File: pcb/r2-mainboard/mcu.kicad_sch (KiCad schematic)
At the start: 28 parts, among them J20 SWD+JTAG (DNP), Q9 AO3400A, SW20 EVQPUC02K, SW21 SW, SW22 SW, U20 STM32G0B1RCT6, Y20 32.768kHz

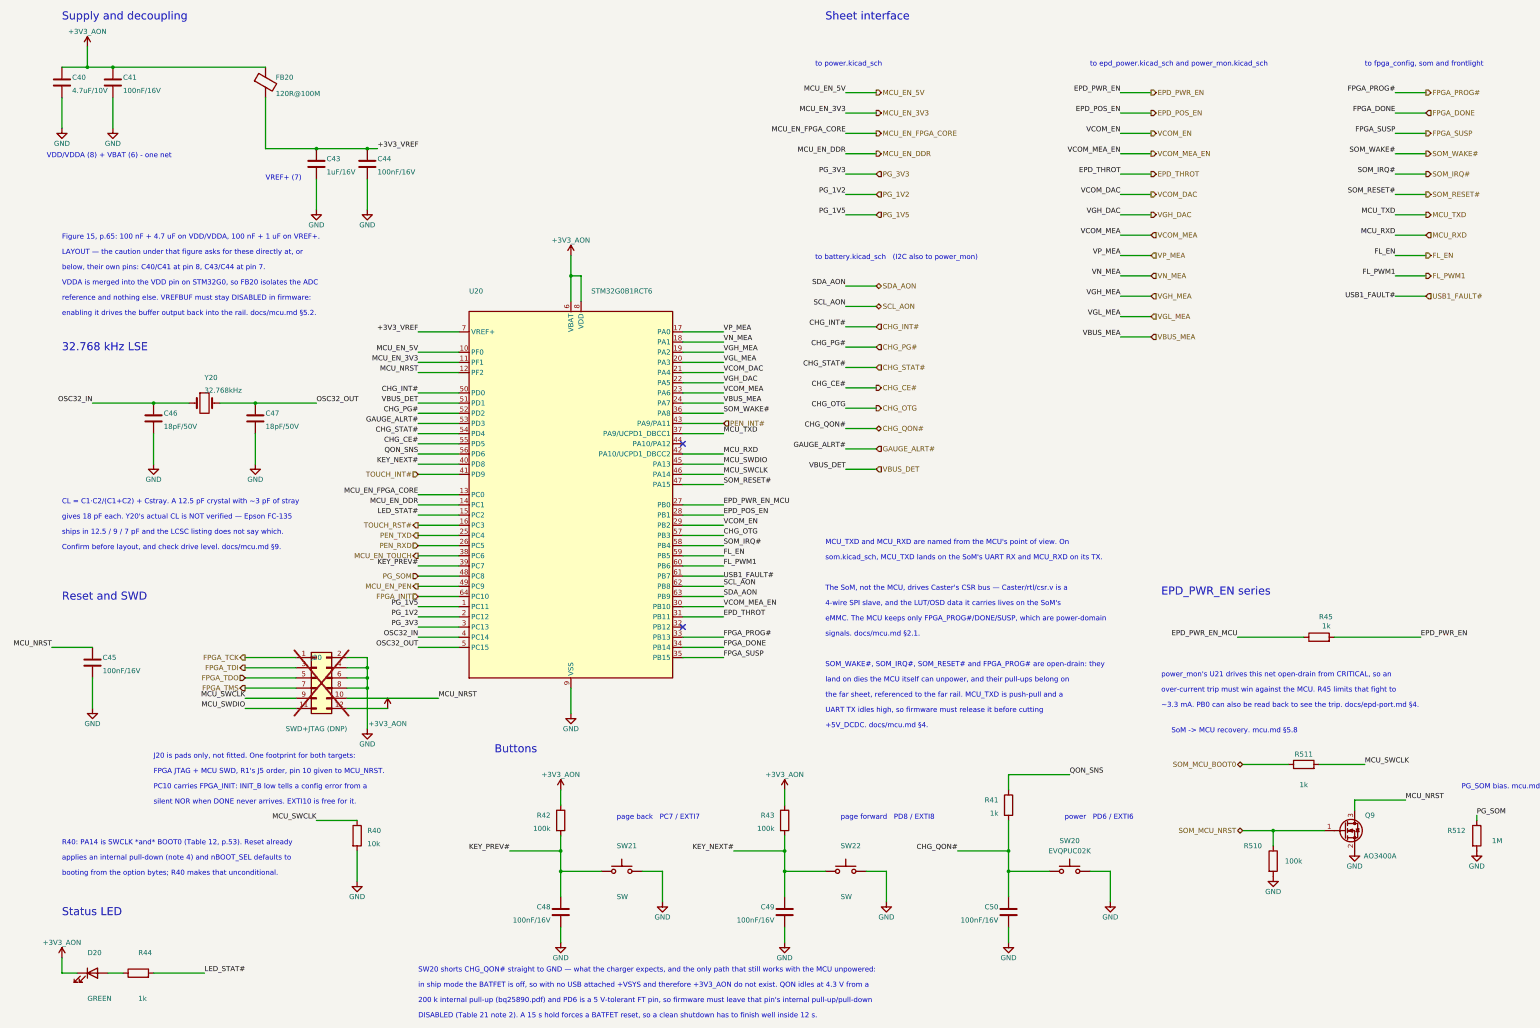
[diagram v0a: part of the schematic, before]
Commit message: R2: renumber every sheet to the page-based designator scheme
The owner's scheme is classifier + sheet page + two-digit part from 00. Four
sheets already used it; this converts the remaining nine, so all thirteen now
agree: pages 2-9 take three digits, pages 10-14 four. 292 of 333 designators
changed. A part shared by several sheets takes its lowest page, so the FPGA is
U700 (pages 7-9) and the two SoM connectors are J501/J502 (pages 5-6).

The whole risk here is silently rewiring the board, so the netlist was diffed
rather than eyeballed:

  nets 519 -> 519, total pin connections 1563 -> 1563
  named nets present in both whose pin multiset changed: 0
  ERC unchanged at 14 errors / 20 warnings
  check_ucf.py: 99 balls matched, 0 failures

That last one matters most: it resolves the gateware's 113 UCF constraints to
board nets *by ball name*, so it is the sharpest detector of the corruption
this change could cause.

Two earlier attempts did cause exactly that. A bare quoted-string substitution
also rewrites FPGA ball names (C1, D2, N11, T1) and BTH-060 pin names (A1-D60),
which are spelled exactly like designators; one run left ERC identical while 40
nets came back with a different pin multiset. The tool now substitutes only at
the two positions that store an instance's designator, and excludes every pin
name everywhere else. docs/layout.md 9.5 records the hazard and how to prove a
renumber was clean.

Only the three scripts that read the design are updated. The gen_*/patch_*/
port_r1.py scripts keep the old names deliberately: each wrote a sheet once and
has not been re-runnable since it was hand-edited in Eeschema, so they are a
historical record -- and port_r1.py's dict keys are R1 designators that were
never renumbered at all.

Co-Authored-By: Claude Opus 5 <noreply@anthropic.com>
Claude-Session: https://claude.ai/code/session_01MHTAe6ZnhogTEgtyPcLhwG
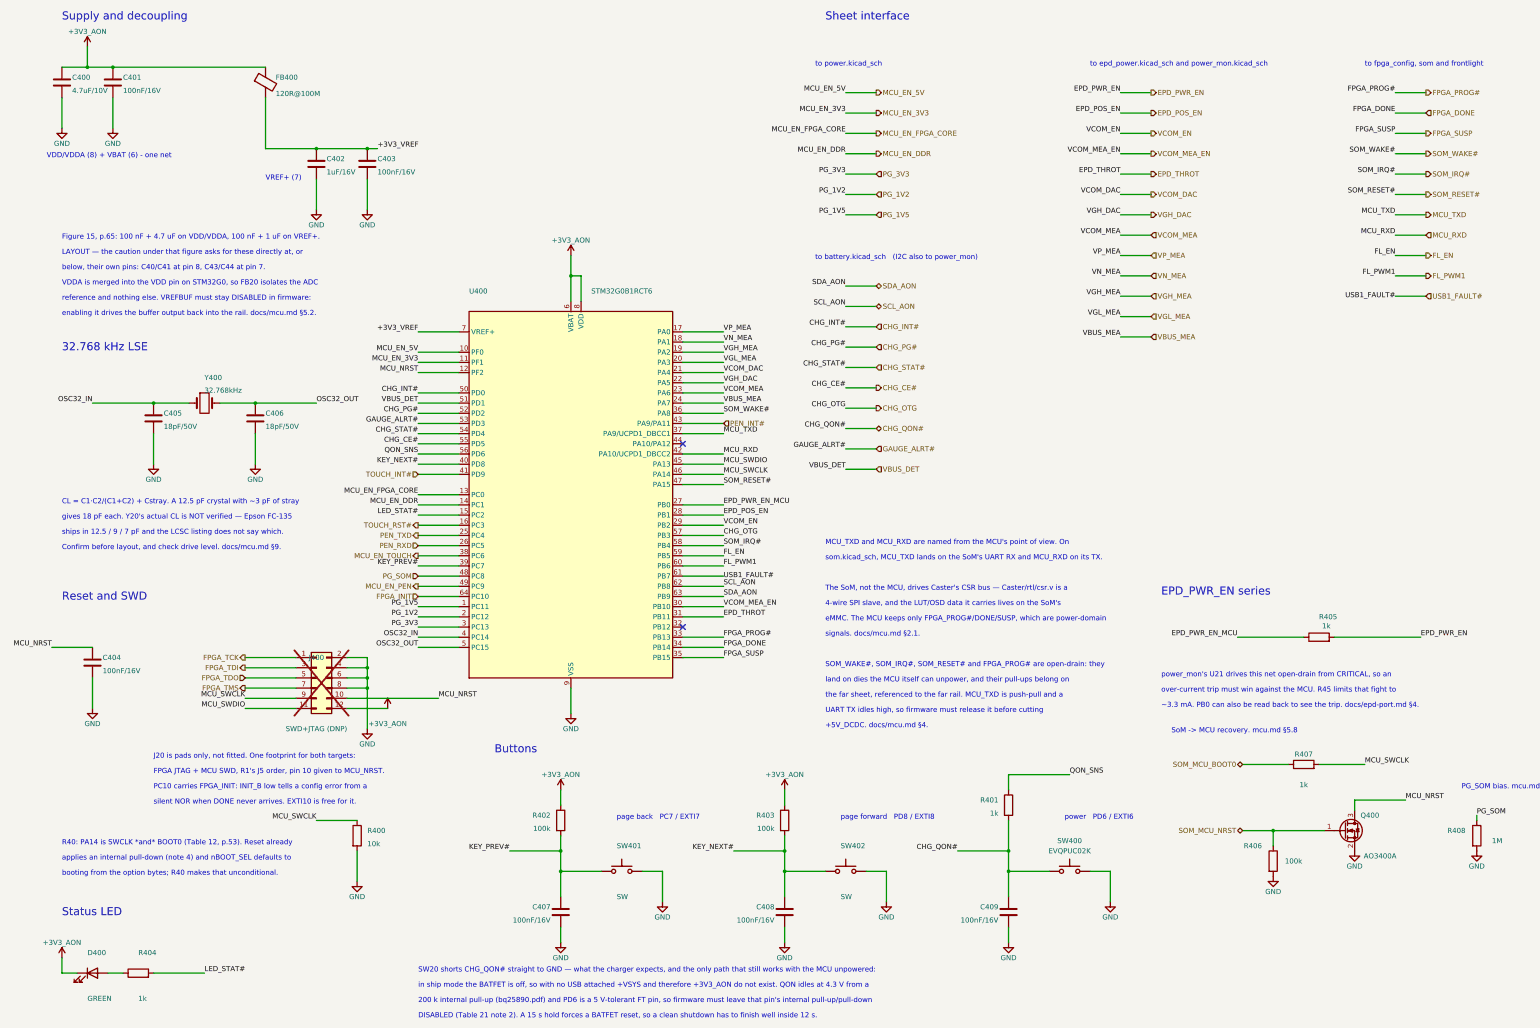
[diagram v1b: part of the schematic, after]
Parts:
- renumbered C40 to C400, C41 to C401, C43 to C402, C44 to C403, C45 to C404, C46 to C405, C47 to C406, C48 to C407, C49 to C408, C50 to C409, D20 to D400, FB20 to FB400, J20 to J400, Q9 to Q400, R40 to R400, R41 to R401, R42 to R402, R43 to R403, R44 to R404, R45 to R405, R510 to R406, R511 to R407, R512 to R408, SW20 to SW400, SW21 to SW401, SW22 to SW402, U20 to U400, Y20 to Y400
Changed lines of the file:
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@@
 		(in_pos_files yes)
 		(dnp no)
-		(property "Reference" "SW21"
+		(property "Reference" "SW401"
 			(at 163.83 240.03 0)
 			(show_name no)
@@
 			(project "r2"
 				(path "/dee825bf-c2f1-415d-afdf-cf702072a6e8/a89f58f8-b115-4f71-9806-30f9bff6e587"
-					(reference "SW21")
+					(reference "SW401")
 					(unit 1)
 				)
@@
 		(in_pos_files yes)
 		(dnp no)
-		(property "Reference" "C46"
+		(property "Reference" "C405"
 			(at 50.8 132.08 0)
 			(show_name no)
@@
 			(project "r2"
 				(path "/dee825bf-c2f1-415d-afdf-cf702072a6e8/a89f58f8-b115-4f71-9806-30f9bff6e587"
-					(reference "C46")
+					(reference "C405")
 					(unit 1)
 				)
@@
 		(in_pos_files yes)
 		(dnp no)
-		(property "Reference" "C43"
+		(property "Reference" "C402"
 			(at 91.44 68.58 0)
 			(show_name no)
@@
 			(project "r2"
 				(path "/dee825bf-c2f1-415d-afdf-cf702072a6e8/a89f58f8-b115-4f71-9806-30f9bff6e587"
-					(reference "C43")
+					(reference "C402")
 					(unit 1)
 				)
@@
 		(in_pos_files yes)
 		(dnp no)
-		(property "Reference" "U20"
+		(property "Reference" "U400"
 			(at 127 101.6 0)
 			(show_name no)
@@
 			(project "r2"
 				(path "/dee825bf-c2f1-415d-afdf-cf702072a6e8/a89f58f8-b115-4f71-9806-30f9bff6e587"
-					(reference "U20")
+					(reference "U400")
 					(unit 1)
 				)
@@
 		(in_pos_files yes)
 		(dnp no)
-		(property "Reference" "Y20"
+		(property "Reference" "Y400"
 			(at 60.96 123.19 0)
 			(show_name no)
@@
 			(project "r2"
 				(path "/dee825bf-c2f1-415d-afdf-cf702072a6e8/a89f58f8-b115-4f71-9806-30f9bff6e587"
-					(reference "Y20")
+					(reference "Y400")
 					(unit 1)
 				)
@@
 		(in_pos_files yes)
 		(dnp no)
-		(property "Reference" "C40"
+		(property "Reference" "C400"
 			(at 27.94 48.26 0)
 			(show_name no)
@@
 			(project "r2"
 				(path "/dee825bf-c2f1-415d-afdf-cf702072a6e8/a89f58f8-b115-4f71-9806-30f9bff6e587"
-					(reference "C40")
+					(reference "C400")
 					(unit 1)
 				)
@@
 		(in_pos_files yes)
 		(dnp no)
-		(property "Reference" "R510"
+		(property "Reference" "R406"
 			(at 322.58 240.03 0)
 			(show_name no)
@@
 			(project "r2"
 				(path "/dee825bf-c2f1-415d-afdf-cf702072a6e8/a89f58f8-b115-4f71-9806-30f9bff6e587"
-					(reference "R510")
+					(reference "R406")
 					(unit 1)
 				)
@@
 		(in_pos_files yes)
 		(dnp no)
-		(property "Reference" "FB20"
+		(property "Reference" "FB400"
 			(at 78.74 48.26 0)
 			(show_name no)
@@
 			(project "r2"
 				(path "/dee825bf-c2f1-415d-afdf-cf702072a6e8/a89f58f8-b115-4f71-9806-30f9bff6e587"
-					(reference "FB20")
+					(reference "FB400")
 					(unit 1)
 				)
@@
 		(in_pos_files yes)
 		(dnp no)
-		(property "Reference" "R45"
+		(property "Reference" "R405"
 			(at 339.09 182.88 270)
 			(show_name no)
@@
 			(project "r2"
 				(path "/dee825bf-c2f1-415d-afdf-cf702072a6e8/a89f58f8-b115-4f71-9806-30f9bff6e587"
-					(reference "R45")
+					(reference "R405")
 					(unit 1)
 				)
@@
 		(in_pos_files yes)
 		(dnp no)
-		(property "Reference" "C50"
+		(property "Reference" "C409"
 			(at 259.08 255.27 0)
 			(show_name no)
@@
 			(project "r2"
 				(path "/dee825bf-c2f1-415d-afdf-cf702072a6e8/a89f58f8-b115-4f71-9806-30f9bff6e587"
-					(reference "C50")
+					(reference "C409")
 					(unit 1)
 				)
@@
 		(in_pos_files yes)
 		(dnp no)
-		(property "Reference" "Q9"
+		(property "Reference" "Q400"
 			(at 351.79 232.41 0)
 			(show_name no)
@@
 			(project "r2"
 				(path "/dee825bf-c2f1-415d-afdf-cf702072a6e8/a89f58f8-b115-4f71-9806-30f9bff6e587"
-					(reference "Q9")
+					(reference "Q400")
 					(unit 1)
 				)
@@
 		(in_pos_files yes)
 		(dnp no)
-		(property "Reference" "C41"
+		(property "Reference" "C401"
 			(at 40.64 48.26 0)
 			(show_name no)
@@
 			(project "r2"
 				(path "/dee825bf-c2f1-415d-afdf-cf702072a6e8/a89f58f8-b115-4f71-9806-30f9bff6e587"
-					(reference "C41")
+					(reference "C401")
 					(unit 1)
 				)
@@
 		(in_pos_files yes)
 		(dnp no)
-		(property "Reference" "R511"
+		(property "Reference" "R407"
 			(at 335.28 217.17 270)
 			(show_name no)
@@
 			(project "r2"
 				(path "/dee825bf-c2f1-415d-afdf-cf702072a6e8/a89f58f8-b115-4f71-9806-30f9bff6e587"
-					(reference "R511")
+					(reference "R407")
 					(unit 1)
 				)
@@
 		(in_pos_files yes)
 		(dnp no)
-		(property "Reference" "SW22"
+		(property "Reference" "SW402"
 			(at 219.71 240.03 0)
 			(show_name no)
@@
 			(project "r2"
 				(path "/dee825bf-c2f1-415d-afdf-cf702072a6e8/a89f58f8-b115-4f71-9806-30f9bff6e587"
-					(reference "SW22")
+					(reference "SW402")
 					(unit 1)
 				)
@@
 		(in_pos_files yes)
 		(dnp no)
-		(property "Reference" "C49"
+		(property "Reference" "C408"
 			(at 203.2 255.27 0)
 			(show_name no)
@@
 			(project "r2"
 				(path "/dee825bf-c2f1-415d-afdf-cf702072a6e8/a89f58f8-b115-4f71-9806-30f9bff6e587"
-					(reference "C49")
+					(reference "C408")
 					(unit 1)
 				)
@@
 		(in_pos_files yes)
 		(dnp no)
-		(property "Reference" "C45"
+		(property "Reference" "C404"
 			(at 35.56 193.04 0)
 			(show_name no)
@@
 			(project "r2"
 				(path "/dee825bf-c2f1-415d-afdf-cf702072a6e8/a89f58f8-b115-4f71-9806-30f9bff6e587"
-					(reference "C45")
+					(reference "C404")
 					(unit 1)
 				)
@@
 		(in_pos_files yes)
 		(dnp no)
-		(property "Reference" "R43"
+		(property "Reference" "R403"
 			(at 203.2 232.41 0)
 			(show_name no)
@@
 			(project "r2"
 				(path "/dee825bf-c2f1-415d-afdf-cf702072a6e8/a89f58f8-b115-4f71-9806-30f9bff6e587"
-					(reference "R43")
+					(reference "R403")
 					(unit 1)
 				)
@@
 		(in_pos_files yes)
 		(dnp no)
-		(property "Reference" "C48"
+		(property "Reference" "C407"
 			(at 147.32 255.27 0)
 			(show_name no)
@@
 			(project "r2"
 				(path "/dee825bf-c2f1-415d-afdf-cf702072a6e8/a89f58f8-b115-4f71-9806-30f9bff6e587"
-					(reference "C48")
+					(reference "C407")
 					(unit 1)
 				)
@@
 		(in_pos_files yes)
 		(dnp no)
-		(property "Reference" "R41"
+		(property "Reference" "R401"
 			(at 259.08 228.6 0)
 			(show_name no)
@@
 			(project "r2"
 				(path "/dee825bf-c2f1-415d-afdf-cf702072a6e8/a89f58f8-b115-4f71-9806-30f9bff6e587"
-					(reference "R41")
+					(reference "R401")
 					(unit 1)
 				)
@@
 		(in_pos_files yes)
 		(dnp no)
-		(property "Reference" "C47"
+		(property "Reference" "C406"
 			(at 76.2 132.08 0)
 			(show_name no)
@@
 			(project "r2"
 				(path "/dee825bf-c2f1-415d-afdf-cf702072a6e8/a89f58f8-b115-4f71-9806-30f9bff6e587"
-					(reference "C47")
+					(reference "C406")
 					(unit 1)
 				)
@@
 		(in_pos_files yes)
 		(dnp no)
-		(property "Reference" "D20"
+		(property "Reference" "D400"
 			(at 31.75 266.7 0)
 			(show_name no)
@@
 			(project "r2"
 				(path "/dee825bf-c2f1-415d-afdf-cf702072a6e8/a89f58f8-b115-4f71-9806-30f9bff6e587"
-					(reference "D20")
+					(reference "D400")
 					(unit 1)
 				)
@@
 		(dnp no)
 		(fields_autoplaced yes)
-		(property "Reference" "SW20"
+		(property "Reference" "SW400"
 			(at 276.86 238.76 0)
 			(show_name no)
@@
 			(project "r2"
 				(path "/dee825bf-c2f1-415d-afdf-cf702072a6e8/a89f58f8-b115-4f71-9806-30f9bff6e587"
-					(reference "SW20")
+					(reference "SW400")
 					(unit 1)
 				)
@@
 		(in_pos_files yes)
 		(dnp no)
-		(property "Reference" "R512"
+		(property "Reference" "R408"
 			(at 373.38 236.22 0)
 			(show_name no)
@@
 			(project "r2"
 				(path "/dee825bf-c2f1-415d-afdf-cf702072a6e8/a89f58f8-b115-4f71-9806-30f9bff6e587"
-					(reference "R512")
+					(reference "R408")
 					(unit 1)
 				)
@@
 		(in_pos_files yes)
 		(dnp no)
-		(property "Reference" "R44"
+		(property "Reference" "R404"
 			(at 44.45 266.7 270)
 			(show_name no)
@@
 			(project "r2"
 				(path "/dee825bf-c2f1-415d-afdf-cf702072a6e8/a89f58f8-b115-4f71-9806-30f9bff6e587"
-					(reference "R44")
+					(reference "R404")
 					(unit 1)
 				)
@@
 		(in_pos_files yes)
 		(dnp yes)
-		(property "Reference" "J20"
+		(property "Reference" "J400"
 			(at 88.9 193.04 0)
 			(show_name no)
@@
 			(project "r2"
 				(path "/dee825bf-c2f1-415d-afdf-cf702072a6e8/a89f58f8-b115-4f71-9806-30f9bff6e587"
-					(reference "J20")
+					(reference "J400")
 					(unit 1)
 				)
@@
 		(in_pos_files yes)
 		(dnp no)
-		(property "Reference" "C44"
+		(property "Reference" "C403"
 			(at 104.14 68.58 0)
 			(show_name no)
@@
 			(project "r2"
 				(path "/dee825bf-c2f1-415d-afdf-cf702072a6e8/a89f58f8-b115-4f71-9806-30f9bff6e587"
-					(reference "C44")
+					(reference "C403")
 					(unit 1)
 				)
@@
 		(in_pos_files yes)
 		(dnp no)
-		(property "Reference" "R42"
+		(property "Reference" "R402"
 			(at 147.32 232.41 0)
 			(show_name no)
@@
 			(project "r2"
 				(path "/dee825bf-c2f1-415d-afdf-cf702072a6e8/a89f58f8-b115-4f71-9806-30f9bff6e587"
-					(reference "R42")
+					(reference "R402")
 					(unit 1)
 				)
@@
 		(in_pos_files yes)
 		(dnp no)
-		(property "Reference" "R40"
+		(property "Reference" "R400"
 			(at 101.6 236.22 0)
 			(show_name no)
@@
 			(project "r2"
 				(path "/dee825bf-c2f1-415d-afdf-cf702072a6e8/a89f58f8-b115-4f71-9806-30f9bff6e587"
-					(reference "R40")
+					(reference "R400")
 					(unit 1)
 				)
